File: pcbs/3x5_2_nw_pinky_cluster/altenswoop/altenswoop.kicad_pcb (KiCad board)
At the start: 2 copper layers, 131 x 89.8 mm, 51 parts, among them J1 TRRS, SW1 Choc, SW10 Choc, SW11 Choc, SW12 Choc, SW13 Choc, SW14 Choc, SW15 Choc, SW16 Choc, SW17 Choc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

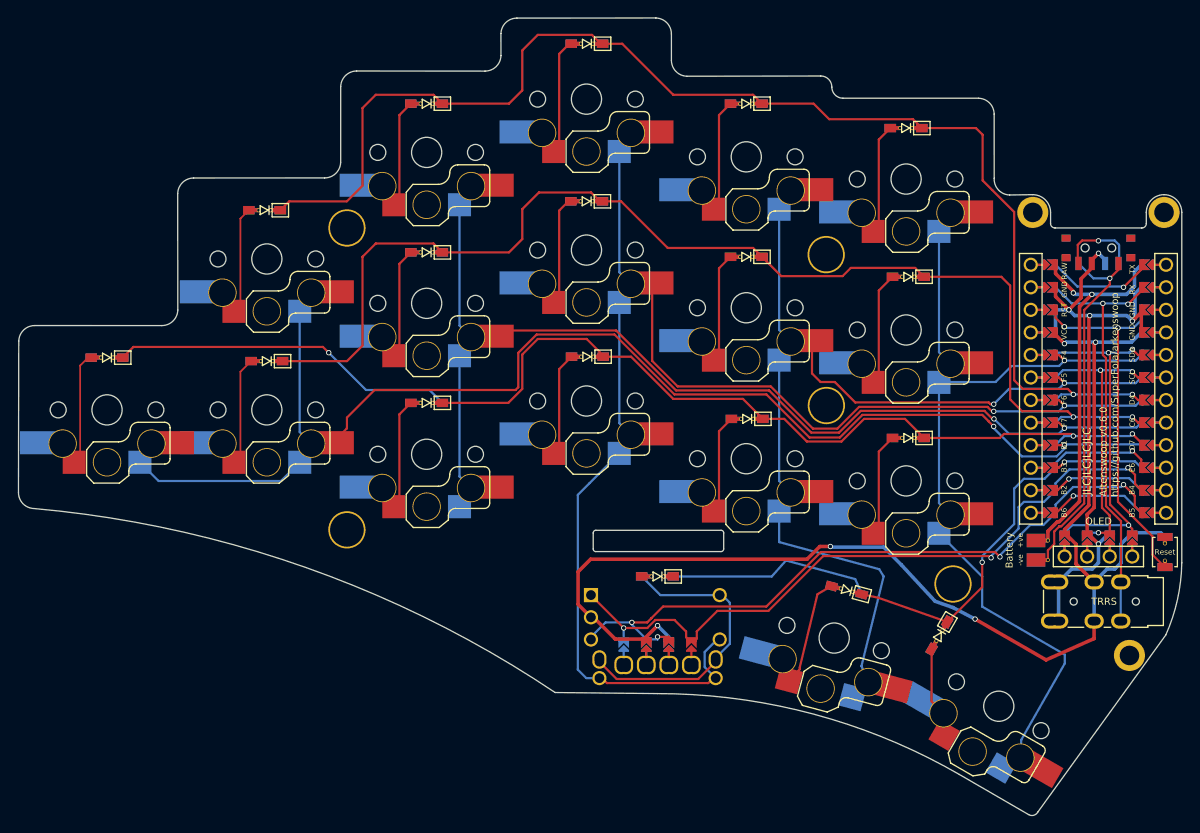
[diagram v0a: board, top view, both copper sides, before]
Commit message: adding the altenswoop
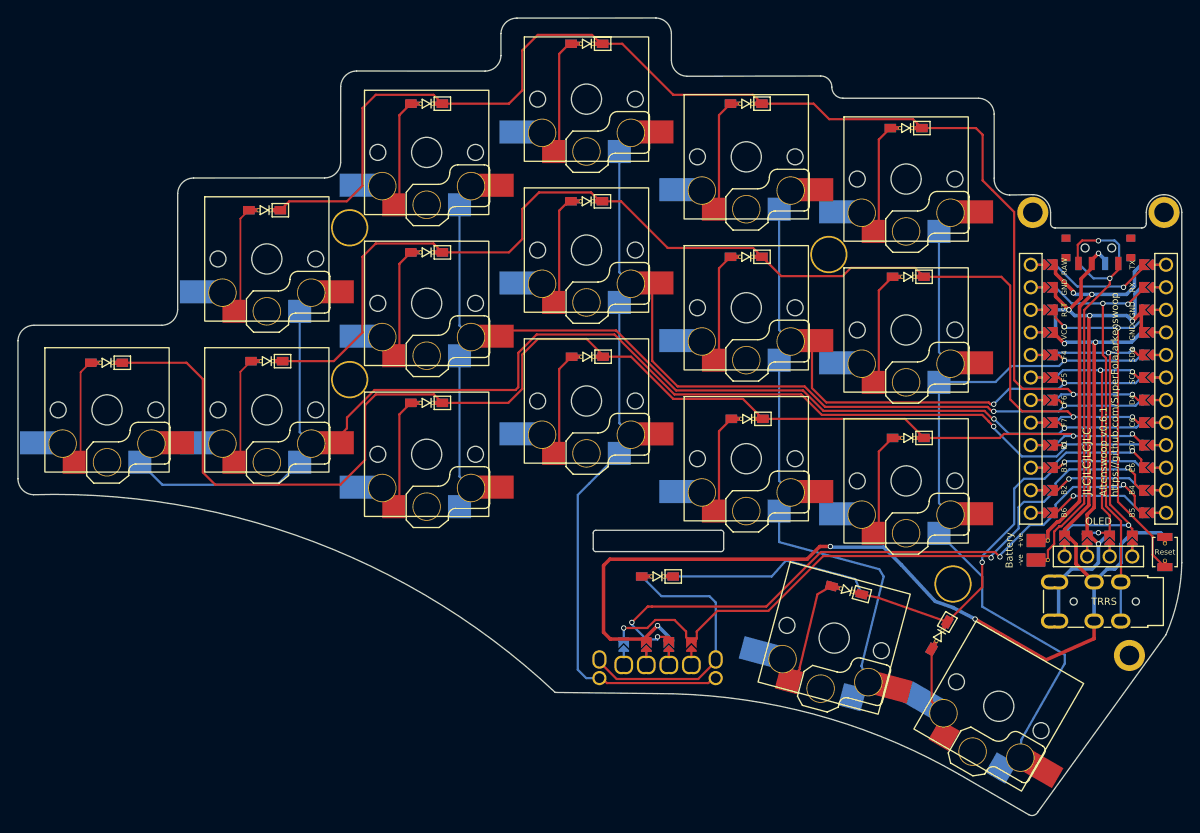
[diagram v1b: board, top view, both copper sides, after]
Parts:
- removed EN1: RotaryEncoder_Switch, swoop:RotaryEncoder
- removed the H4 at (134.2, 103.8)
- BT1: footprint swoop:Battery_pads_reversible -> arkenswoop:Battery_pads_reversible
- D1, D10, D11, D12, D13, D14, D15, D16, D17, D2, D3, D4, D5, D6, D7, D8, D9, ED1: footprint swoop:D3_SMD -> arkenswoop:D3_SMD
- EN2: footprint swoop:RollerEncoder -> arkenswoop:RollerEncoder
- H1, H2, H3, H4: footprint swoop:M2_hole_4.2mm -> arkenswoop:M2_hole_4.2mm
- J1: footprint swoop:TRRS-3pin -> arkenswoop:TRRS-3pin
- O1: footprint swoop:OLED_jumpers -> arkenswoop:OLED_jumpers
- PSW1: footprint swoop:Power -> arkenswoop:Power
- RSW1: footprint swoop:Reset -> arkenswoop:Reset
- Ref** (x2): footprint chocolad:M2_hole_3.5mm -> arkenswoop:M2_hole_3.5mm
- Ref**: footprint swoop:M2_hole_3.5mm -> arkenswoop:M2_hole_3.5mm
- SW1, SW10, SW11, SW12, SW13, SW14, SW15, SW16, SW17, SW2, SW3, SW4, SW5, SW6, SW7, SW8, SW9: footprint Library:Kailh-pg1350-socket-reversible -> arkenswoop:Kailh-pg1350-socket-reversible
- U1: footprint swoop:ProMicro_jumpers -> arkenswoop:ProMicro_jumpers
- moved H2 16.9 mm to (80.6, 100.8)
- moved D11 0.58 mm to (53.2, 98.9)
- moved H1 0.31 mm to (80.6, 83.7)
- moved H3 0.30 mm to (134.5, 86.7)
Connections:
- D10 pad 2: Net-(D10-A) -> (no net)
- D12 pad 2: Net-(D12-A) -> (no net)
- D13 pad 2: Net-(D13-A) -> (no net)
- D14 pad 2: Net-(D14-A) -> (no net)
- D15 pad 2: Net-(D15-A) -> (no net)
- D16 pad 2: Net-(D16-A) -> (no net)
- D17 pad 2: Net-(D17-A) -> (no net)
- D2 pad 2: Net-(D2-A) -> (no net)
- D3 pad 2: Net-(D3-A) -> (no net)
- D4 pad 2: Net-(D4-A) -> (no net)
- D5 pad 2: Net-(D5-A) -> (no net)
- D7 pad 2: Net-(D7-A) -> (no net)
- D8 pad 2: Net-(D8-A) -> (no net)
- D9 pad 2: Net-(D9-A) -> (no net)
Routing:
- net row2: track 133.4 -> 148.2 mm, vias 3 -> 2
- net col2: track 149.8 -> 141.9 mm
- net eda: track 78.8 -> 73.3 mm
- net edb: track 77.9 -> 72.6 mm
- net GND: track 164.2 -> 160.6 mm
- net er0: track 33.7 -> 31.3 mm
- net col1: track 112.9 -> 110.8 mm
- net col0: track 144.0 -> 142.3 mm
- net col3: track 104.1 -> 105.1 mm
- net row1: track 134.2 -> 133.4 mm
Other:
- board size 131 x 89.8 mm -> 131.1 x 89.8 mm
